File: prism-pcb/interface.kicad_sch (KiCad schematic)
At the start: 8 parts, among them J301 FFC_P1mm_BOT_RA_SMD, M301 Fan_5VDC_25x25x8mm, U301 TPSM365R6V5RDNR

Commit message: Update metadata
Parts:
- U301: Package (none) -> QFN-11(3.5x4.5); Synopsis 3-V TO 65-V INPUT, 1-V TO 13-V O -> DC-DC 5V 600mA Output 3-65V Input
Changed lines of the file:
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@@
       (effects (font (size 1.27 1.27) italic) hide)
     )
-    (property "Synopsis" "3-V TO 65-V INPUT, 1-V TO 13-V O" (at 193.04 43.18 0)
+    (property "Synopsis" "DC-DC 5V 600mA Output 3-65V Input" (at 193.04 43.18 0)
       (effects (font (size 1.27 1.27)) hide)
     )
@@
       (effects (font (size 1.27 1.27)) hide)
     )
+    (property "Package" "QFN-11(3.5x4.5)" (at 193.04 68.58 0)
+      (effects (font (size 1.27 1.27)) hide)
+    )

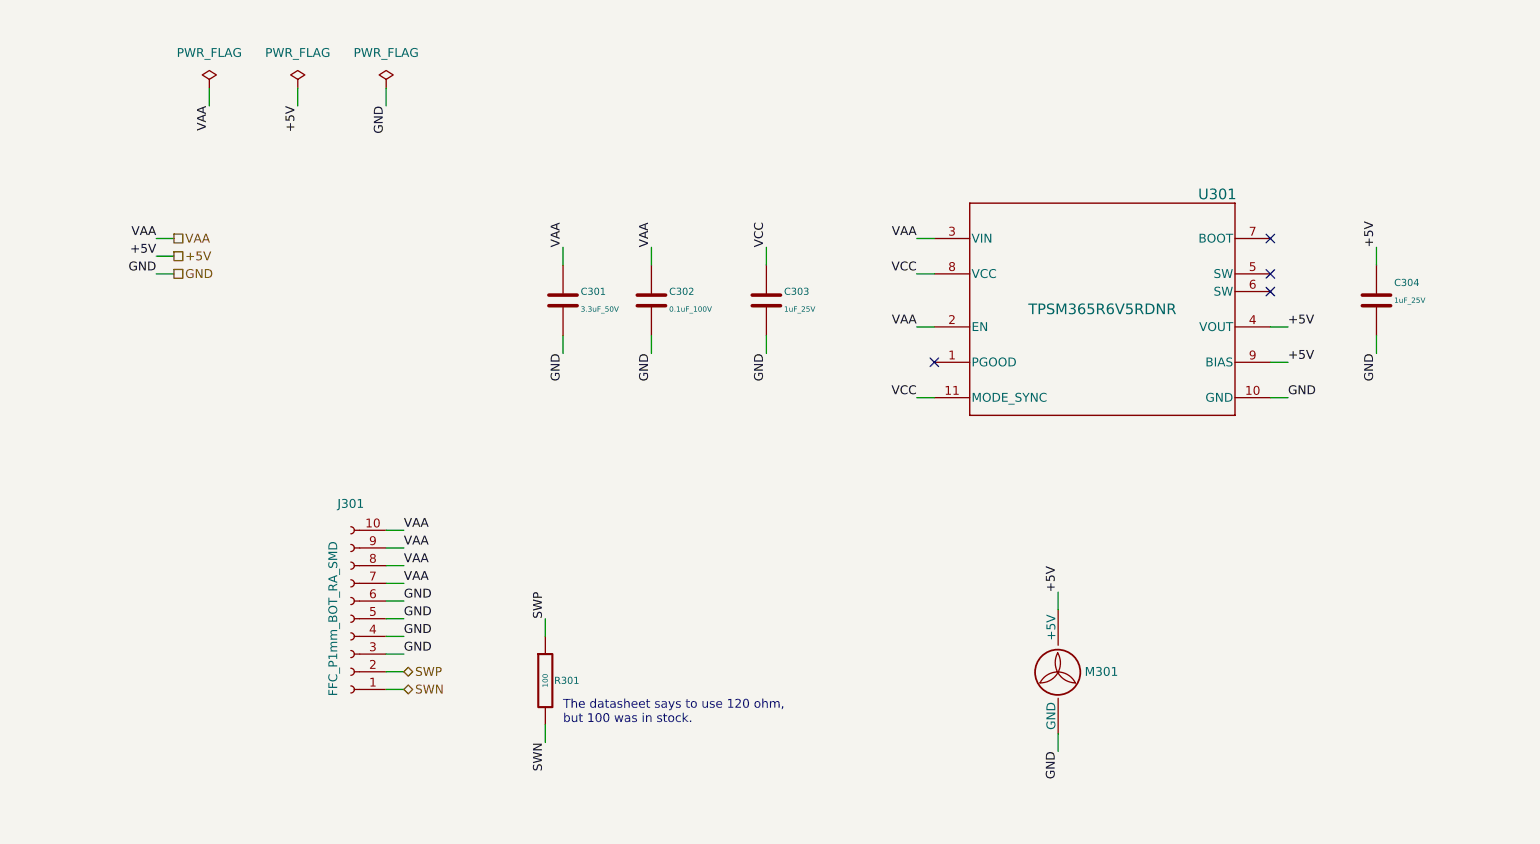
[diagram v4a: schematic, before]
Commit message: Change to 5V xtal, add capacitors and led, use TMC5130 5V external
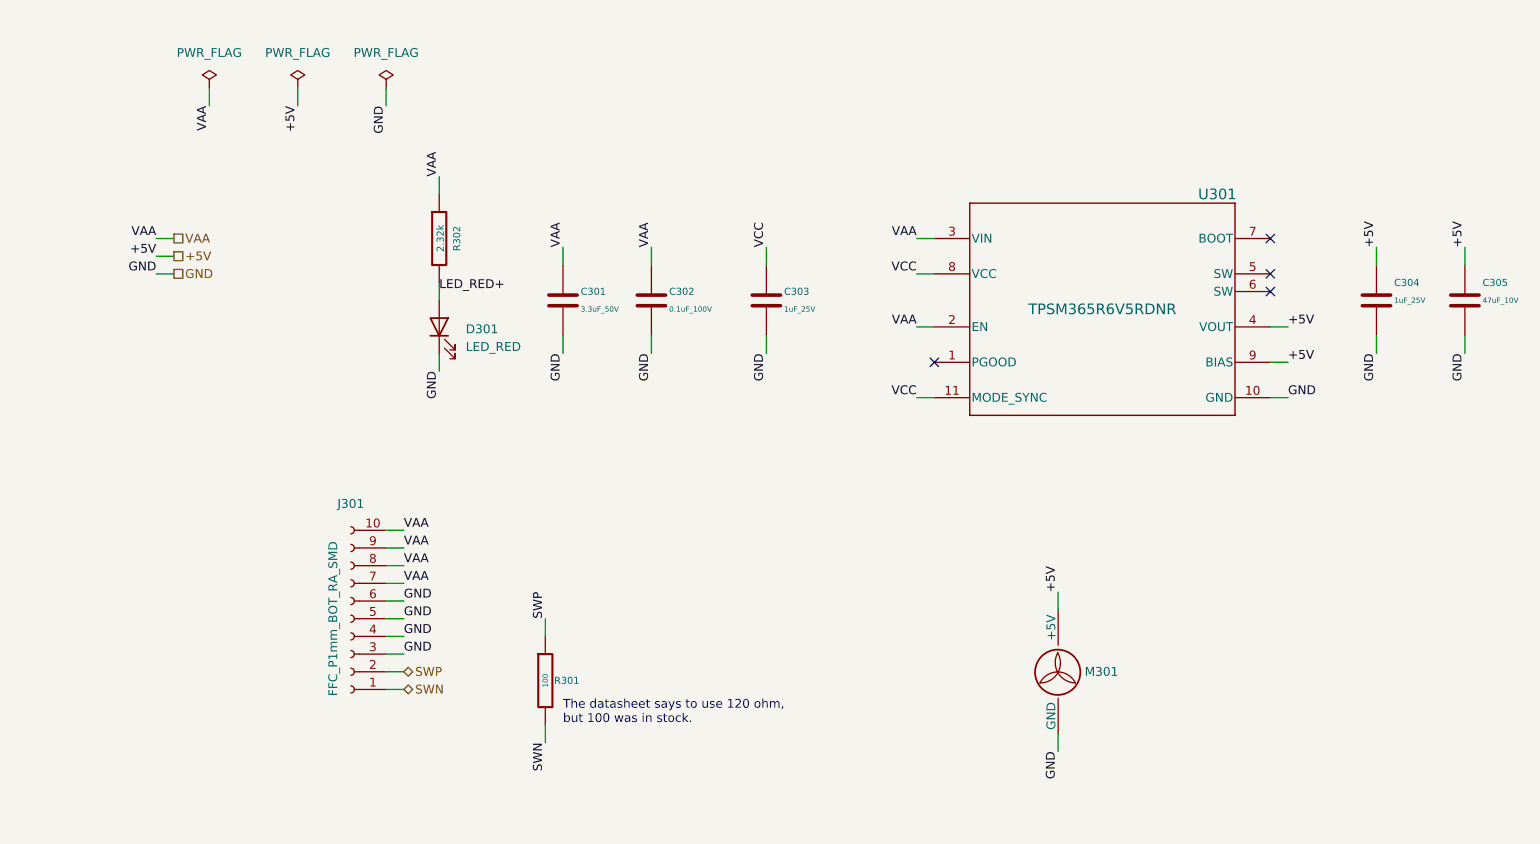
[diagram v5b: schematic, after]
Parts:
- added C305: 47uF_10V, Janelia:C_0805_2012Metric, symbol Janelia:C_47uF_10V_0805
- added D301: LED_RED, Janelia:LED_0402-1005_KNB, symbol Janelia:LED_KNB_20mA_RED_1.95V_0402
- added R302: 2.32k, Janelia:R_0805_2012Metric, symbol Janelia:R_2.32k_1W_0805
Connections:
- net +5V: now also C305.1
- net GND: now also C305.2, D301.1 (K)
- net VAA: now also R302.1
- new net LED_RED+: D301.2 (A), R302.2
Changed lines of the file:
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@@
   (title_block
     (title "prism-pcb")
-    (date "2024-08-07")
+    (date "2024-08-22")
     (rev "1.2")
     (company "Howard Hughes Medical Institute")
@@
     (stroke (width 0) (type default))
   )
+  (wire (pts (xy 245.11 72.39) (xy 245.11 74.93))
+    (stroke (width 0) (type default))
+  )
   (wire (pts (xy 59.69 63.5) (xy 57.15 63.5))
     (stroke (width 0) (type default))
@@
     (stroke (width 0) (type default))
   )
+  (wire (pts (xy 245.11 62.23) (xy 245.11 59.69))
+    (stroke (width 0) (type default))
+  )
   (wire (pts (xy 128.27 72.39) (xy 128.27 74.93))
     (stroke (width 0) (type default))
@@
     (stroke (width 0) (type default))
   )
+  (wire (pts (xy 97.79 74.93) (xy 97.79 77.47))
+    (stroke (width 0) (type default))
+  )
   (wire (pts (xy 232.41 72.39) (xy 232.41 74.93))
     (stroke (width 0) (type default))
   )
+  (wire (pts (xy 97.79 64.77) (xy 97.79 67.31))
+    (stroke (width 0) (type default))
+  )
   (wire (pts (xy 113.03 115.57) (xy 113.03 113.03))
     (stroke (width 0) (type default))
@@
   )
   (wire (pts (xy 90.17 100.33) (xy 92.71 100.33))
+    (stroke (width 0) (type default))
+  )
+  (wire (pts (xy 97.79 52.07) (xy 97.79 49.53))
     (stroke (width 0) (type default))
   )
@@
     (effects (font (size 1.27 1.27)) (justify left bottom))
   )
+  (label "+5V" (at 245.11 59.69 90) (fields_autoplaced)
+    (effects (font (size 1.27 1.27)) (justify left bottom))
+  )
   (label "VCC" (at 166.37 63.5 180) (fields_autoplaced)
     (effects (font (size 1.27 1.27)) (justify right bottom))
@@
     (effects (font (size 1.27 1.27)) (justify left bottom))
   )
+  (label "GND" (at 97.79 77.47 270) (fields_autoplaced)
+    (effects (font (size 1.27 1.27)) (justify right bottom))
+  )
+  (label "GND" (at 245.11 74.93 270) (fields_autoplaced)
+    (effects (font (size 1.27 1.27)) (justify right bottom))
+  )
   (label "VAA" (at 57.15 58.42 180) (fields_autoplaced)
     (effects (font (size 1.27 1.27)) (justify right bottom))
@@
     (effects (font (size 1.27 1.27)) (justify right bottom))
   )
+  (label "VAA" (at 97.79 49.53 90) (fields_autoplaced)
+    (effects (font (size 1.27 1.27)) (justify left bottom))
+  )
   (label "+5V" (at 219.71 76.2 0) (fields_autoplaced)
     (effects (font (size 1.27 1.27)) (justify left bottom))
@@
   )
   (label "GND" (at 92.71 110.49 0) (fields_autoplaced)
+    (effects (font (size 1.27 1.27)) (justify left bottom))
+  )
+  (label "LED_RED+" (at 97.79 66.04 0) (fields_autoplaced)
     (effects (font (size 1.27 1.27)) (justify left bottom))
   )
@@
         (path "/df2b2e89-e055-4140-95de-f1df723db034/c1dd8f61-494c-402f-8e59-08309c64fc3f"
           (reference "#FLG0303") (unit 1)
+        )
+      )
+    )
+  )
+  (symbol (lib_id "Janelia:C_47uF_10V_0805") (at 245.11 67.31 0) (unit 1)
+    (in_bom yes) (on_board yes) (dnp no)
+    (property "Reference" "C305" (at 247.65 64.77 0)
+      (effects (font (size 1.016 1.016)) (justify left))
+    )
+    (property "Value" "47uF_10V" (at 247.65 67.31 0)
+      (effects (font (size 0.762 0.762)) (justify left))
+    )
+    (property "Footprint" "Janelia:C_0805_2012Metric" (at 246.0752 71.12 0)
+      (effects (font (size 0.762 0.762)) hide)
+    )
+    (property "Datasheet" "" (at 245.11 67.31 0)
+      (effects (font (size 1.524 1.524)))
+    )
+    (property "Vendor" "Digi-Key" (at 247.65 62.23 0)
+      (effects (font (size 1.524 1.524)) hide)
+    )
+    (property "Vendor Part Number" "445-8239-1-ND" (at 250.19 59.69 0)
+      (effects (font (size 1.524 1.524)) hide)
+    )
+    (property "Package" "0805" (at 245.11 67.31 0)
+      (effects (font (size 1.27 1.27)) hide)
+    )
+    (property "Manufacturer" "TDK Corporation" (at 245.11 67.31 0)
+      (effects (font (size 1.27 1.27)) hide)
+    )
+    (property "Manufacturer Part Number" "C2012X5R1A476M125AC" (at 245.11 67.31 0)
+      (effects (font (size 1.27 1.27)) hide)
+    )
+    (property "Synopsis" "CAP CER 47UF 10V X5R" (at 252.73 57.15 0)
+      (effects (font (size 1.524 1.524)) hide)
+    )
+    (property "LCSC" "C2182652" (at 245.11 67.31 0)
+      (effects (font (size 1.27 1.27)) hide)
+    )
+    (pin "2")
+    (pin "1")
+    (instances
+      (project "prism-pcb"
+        (path "/df2b2e89-e055-4140-95de-f1df723db034/c1dd8f61-494c-402f-8e59-08309c64fc3f"
+          (reference "C305") (unit 1)
         )
       )
@@
     )
   )
+  (symbol (lib_id "Janelia:R_2.32k_1W_0805") (at 97.79 58.42 0) (unit 1)
+    (in_bom yes) (on_board yes) (dnp no)
+    (property "Reference" "R302" (at 100.33 58.42 90)
+      (effects (font (size 1.016 1.016)))
+    )
+    (property "Value" "2.32k" (at 97.9678 58.3946 90) (do_not_autoplace)
+      (effects (font (size 1.016 1.016)))
+    )
+    (property "Footprint" "Janelia:R_0805_2012Metric" (at 96.012 58.42 90)
+      (effects (font (size 0.762 0.762)) hide)
+    )
+    (property "Datasheet" "" (at 97.79 58.42 0)
+      (effects (font (size 0.762 0.762)))
+    )
+    (property "Package" "0805" (at 97.79 58.42 0)
+      (effects (font (size 1.524 1.524)) hide)
+    )
+    (property "Manufacturer" "TE Connectivity Passive Product" (at 97.79 58.42 0)
+      (effects (font (size 1.524 1.524)) hide)
+    )
+    (property "Manufacturer Part Number" "RA73F2A2K32BTD" (at 97.79 58.42 0)
+      (effects (font (size 1.524 1.524)) hide)
+    )
+    (property "Vendor" "Digi-Key" (at 97.79 58.42 0)
+      (effects (font (size 1.524 1.524)) hide)
+    )
+    (property "Vendor Part Number" "1712-RA73F2A2K32BTDCT-ND" (at 97.79 58.42 0)
+      (effects (font (size 1.524 1.524)) hide)
+    )
+    (property "Synopsis" "RA73F 2A 2K32 0.1% 5K RL" (at 107.442 50.8 90)
+      (effects (font (size 1.524 1.524)) hide)
+    )
+    (property "LCSC" "C3961061" (at 97.79 58.42 0)
+      (effects (font (size 1.27 1.27)) hide)
+    )
+    (pin "2")
+    (pin "1")
+    (instances
+      (project "prism-pcb"
+        (path "/df2b2e89-e055-4140-95de-f1df723db034/c1dd8f61-494c-402f-8e59-08309c64fc3f"
+          (reference "R302") (unit 1)
+        )
+      )
+    )
+  )
   (symbol (lib_id "Janelia:C_0.1uF_100V_0402") (at 128.27 67.31 0) (unit 1)
     (in_bom yes) (on_board yes) (dnp no)
@@
         )
       )
+    )
+  )
+  (symbol (lib_id "Janelia:LED_KNB_20mA_RED_1.95V_0402") (at 97.79 71.12 90) (unit 1)
+    (in_bom yes) (on_board yes) (dnp no)
+    (property "Reference" "D301" (at 101.6 71.4375 90)
+      (effects (font (size 1.27 1.27)) (justify right))
+    )
+    (property "Value" "LED_RED" (at 101.6 73.9775 90)
+      (effects (font (size 1.27 1.27)) (justify right))
+    )
+    (property "Footprint" "Janelia:LED_0402-1005_KNB" (at 88.9 71.12 0)
+      (effects (font (size 1.27 1.27)) hide)
+    )
+    (property "Datasheet" "~" (at 90.17 71.12 0)
+      (effects (font (size 1.27 1.27)) hide)
+    )
+    (property "Synopsis" "LED RED CLEAR CHIP SMD" (at 76.2 71.12 0)
+      (effects (font (size 1.27 1.27)) hide)
+    )
+    (property "Package" "0402" (at 86.36 71.12 0)
+      (effects (font (size 1.27 1.27)) hide)
+    )
+    (property "Manufacturer" "Kingbright" (at 81.28 71.12 0)
+      (effects (font (size 1.27 1.27)) hide)
+    )
+    (property "Manufacturer Part Number" "APHHS1005SURCK" (at 78.74 71.12 0)
+      (effects (font (size 1.27 1.27)) hide)
+    )
+    (property "Vendor" "Digi-Key" (at 91.44 71.12 0)
+      (effects (font (size 1.27 1.27)) hide)
+    )
+    (property "Vendor Part Number" "754-1104-1-ND" (at 83.82 71.12 0)
+      (effects (font (size 1.27 1.27)) hide)
+    )
+    (property "LCSC" "C2852592" (at 73.66 71.12 0)
+      (effects (font (size 1.27 1.27)) hide)
+    )
+    (pin "2")
+    (pin "1")
+    (instances
+      (project "prism-pcb"
+        (path "/df2b2e89-e055-4140-95de-f1df723db034/c1dd8f61-494c-402f-8e59-08309c64fc3f"
+          (reference "D301") (unit 1)
+        )
+      )

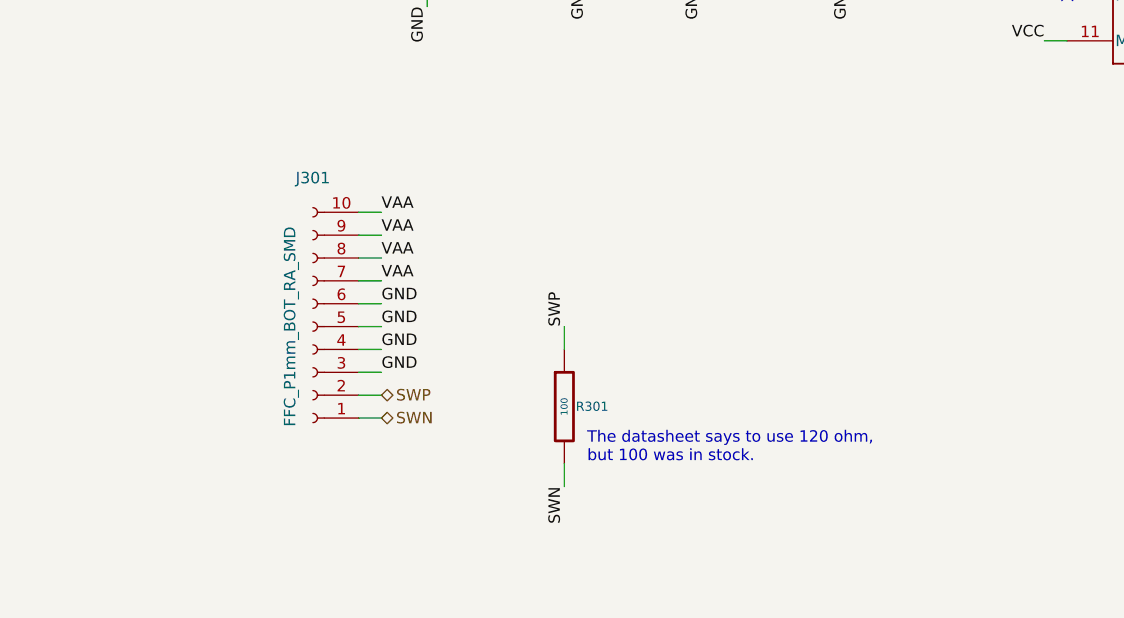
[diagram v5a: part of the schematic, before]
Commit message: Change connector and add diode
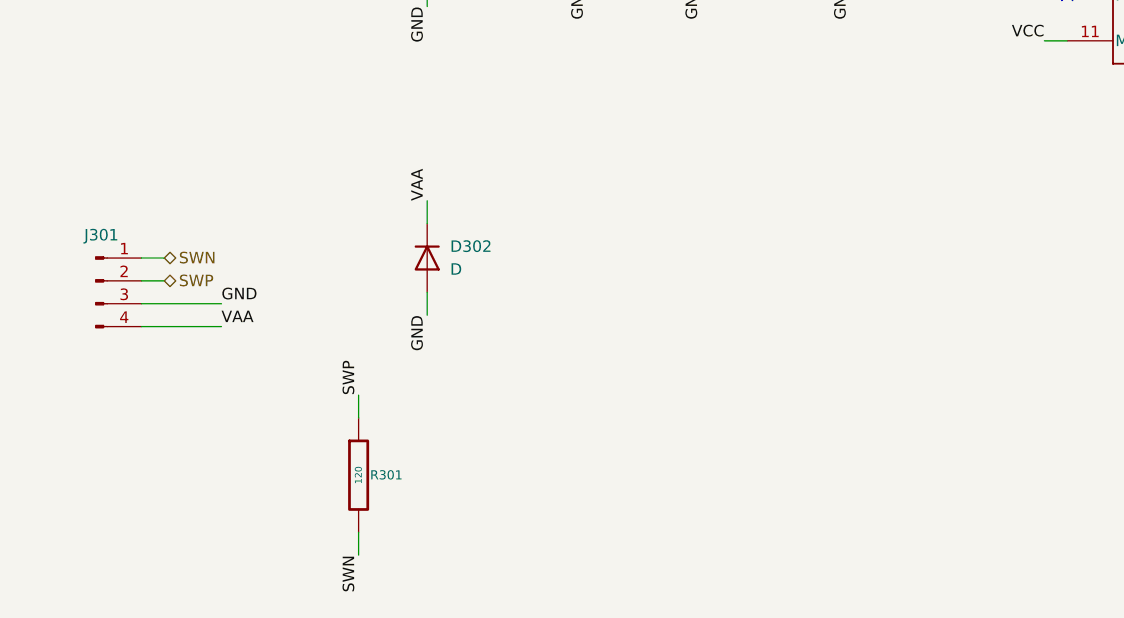
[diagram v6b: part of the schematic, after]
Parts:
- removed J301: FFC_P1mm_BOT_RA_SMD, Janelia:CONN_C2914097, symbol Janelia:Conn_01x10_FFC_P1mm_BOT_RA_SMD
- removed R301: 100, Janelia:R_0402_1005Metric, symbol Janelia:R_100_0402
- added D302: D, Janelia:D_SMA, symbol Janelia:D_2A_200V_SMA
- added J301: Conn_01x04_P3.5mm_TBH_Horizontal_Screw, Janelia:PhoenixContact_MC_1,5_4-G-3.5_1x04_P3.50mm_Horizontal_Screw, symbol Janelia:Conn_01x04_P3.5mm_TBH_Horizontal_Screw
- added R301: 120, Janelia:R_0402_1005Metric, symbol Janelia:R_120_0402
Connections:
- net GND: now also D302.2 (A), J301.3 (Pin_3)
- net SWN: now also J301.1 (Pin_1), R301.2
- net SWP: now also J301.2 (Pin_2), R301.1
- net VAA: now also D302.1 (K), J301.4 (Pin_4)
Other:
- note removed: "The datasheet says to use 120 ohm, but 100 was in stock."

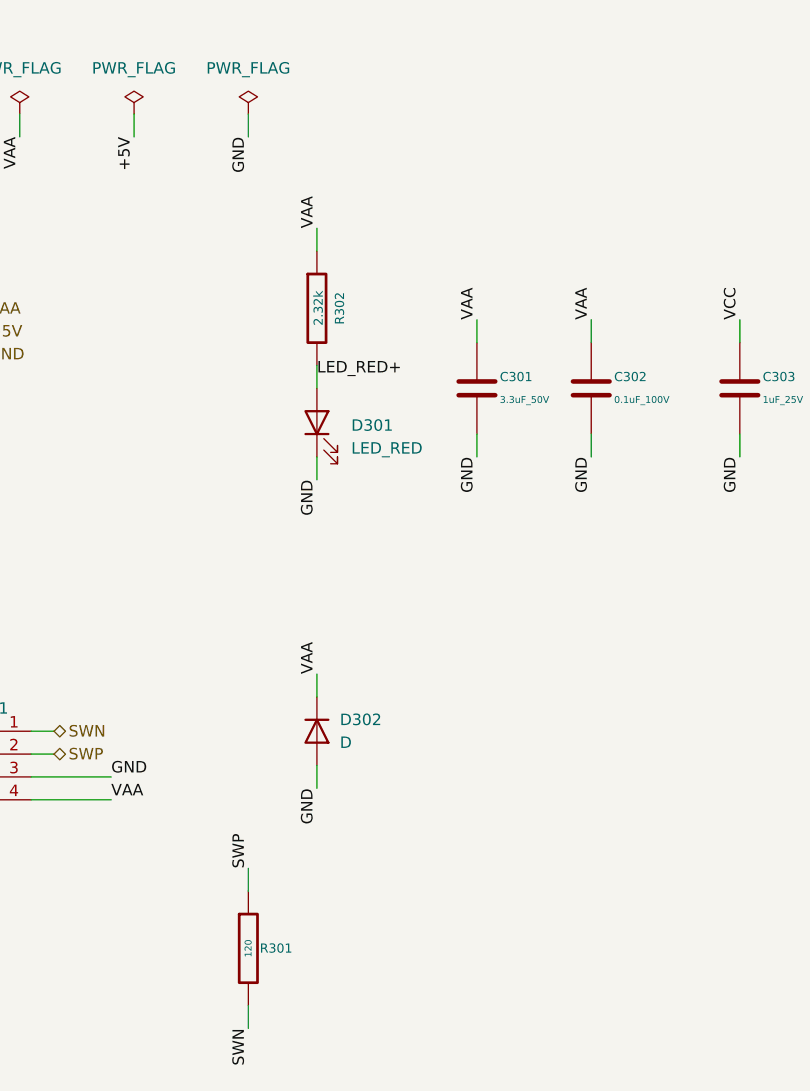
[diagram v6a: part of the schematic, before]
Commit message: Changed connector, added uart pullup, grounded more pins
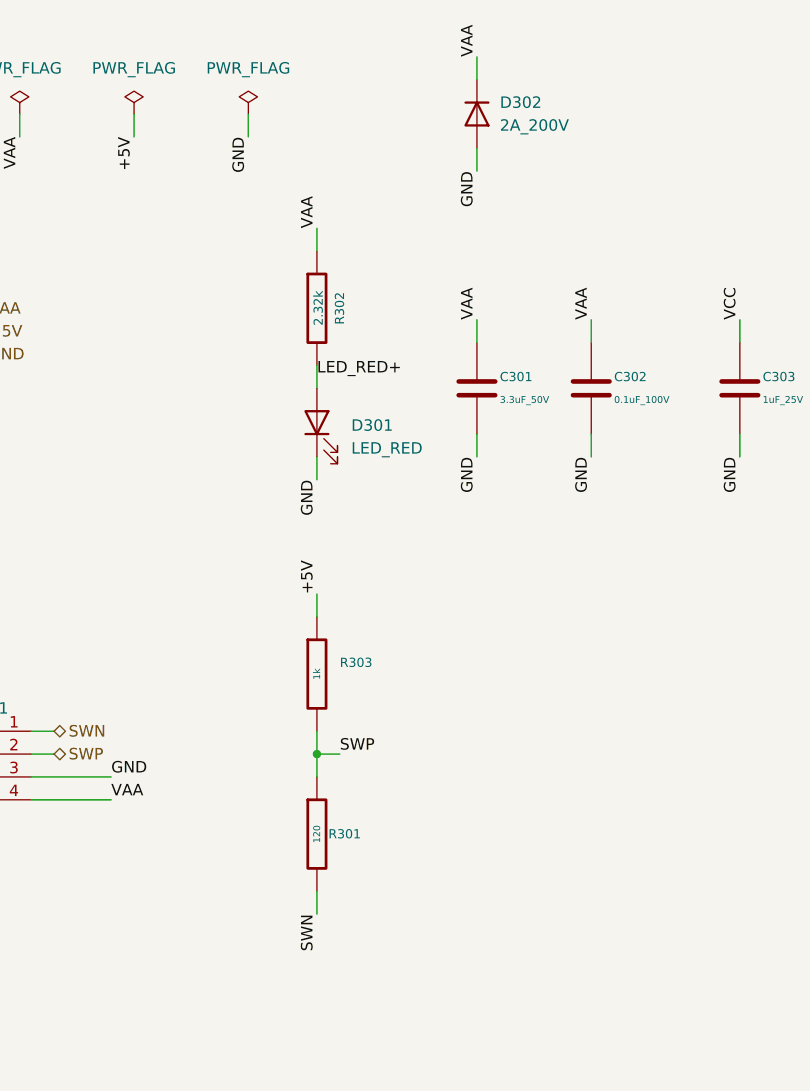
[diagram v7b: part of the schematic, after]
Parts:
- added R303: 1k, Janelia:R_0402_1005Metric, symbol Janelia:R_1k_0402
- D302: value D -> 2A_200V
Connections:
- net +5V: now also R303.1
- net SWP: now also R303.2
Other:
- moved on the sheet: D302, R301
